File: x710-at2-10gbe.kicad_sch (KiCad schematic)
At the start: 18 parts, among them U4 EZX710AT2_S_LMR5

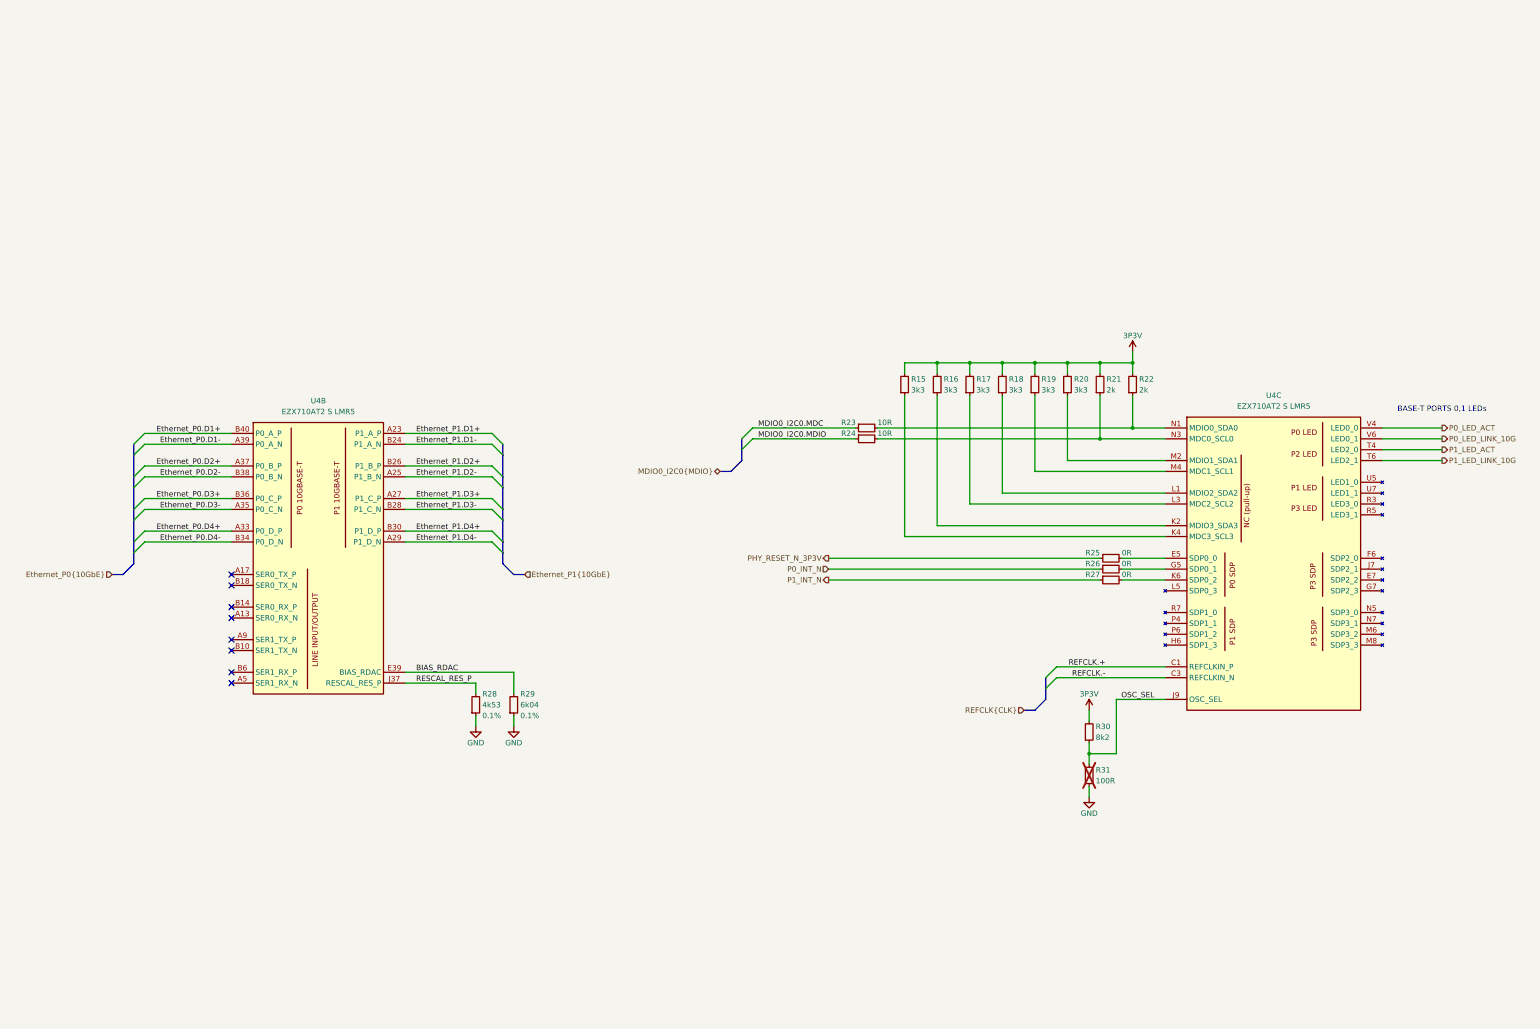
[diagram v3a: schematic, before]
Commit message: [#80813] Improve schematic readability, add debug connectors and missing resistors
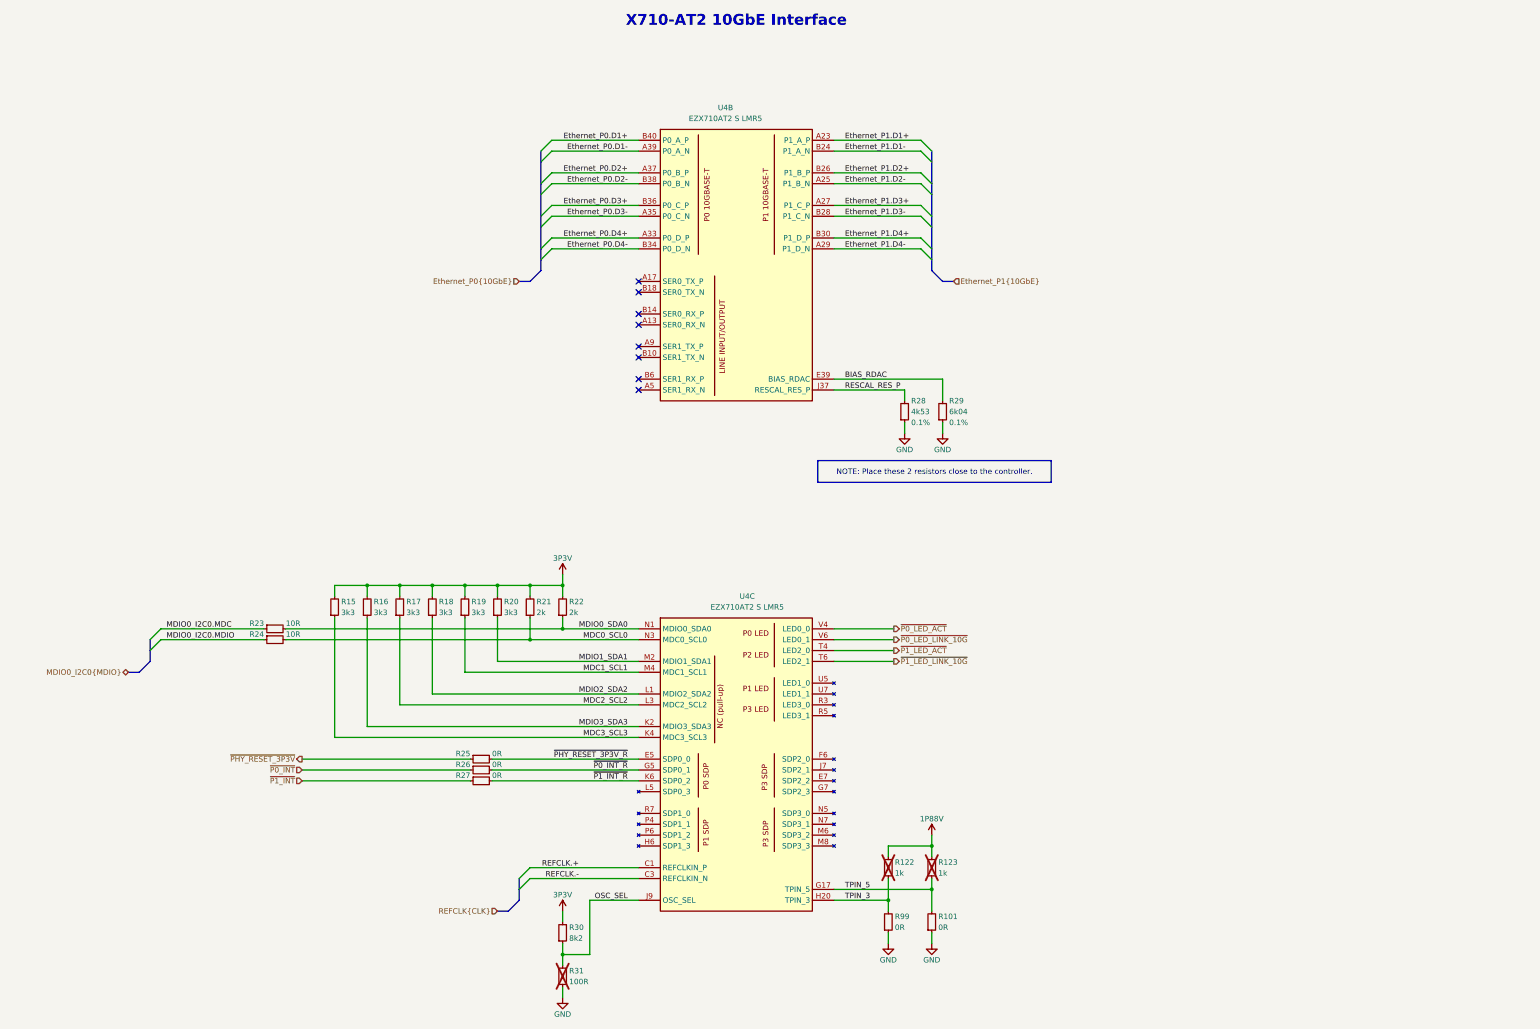
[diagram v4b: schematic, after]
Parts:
- added R101, R99: R_0R_0402, antmicro-footprints:R_0402_1005Metric, symbol antmicroResistors0402:R_0R_0402
- added R122, R123: R_1k_0402, antmicro-footprints:R_0402_1005Metric, symbol antmicroResistors0402:R_1k_0402
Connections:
- net GND: now also R101.1, R99.1
- net ~{P1_INT_R}: now reaches R27.2, U4.K6 (SDP0_2)
- net MDC1_SCL1: now reaches R19.1, U4.M4 (MDC1_SCL1)
- net ~{P0_INT_R}: now reaches R26.2, U4.G5 (SDP0_1)
- net MDC0_SCL0: now reaches R21.1, R24.2, U4.N3 (MDC0_SCL0)
- net MDIO0_SDA0: now reaches R22.1, R23.2, U4.N1 (MDIO0_SDA0)
- net MDIO2_SDA2: now reaches R18.1, U4.L1 (MDIO2_SDA2)
- net ~{PHY_RESET_3P3V_R}: now reaches R25.2, U4.E5 (SDP0_0)
- net MDIO3_SDA3: now reaches R16.1, U4.K2 (MDIO3_SDA3)
- net MDC3_SCL3: now reaches R15.1, U4.K4 (MDC3_SCL3)
- net MDC2_SCL2: now reaches R17.1, U4.L3 (MDC2_SCL2)
- net MDIO1_SDA1: now reaches R20.1, U4.M2 (MDIO1_SDA1)
- net P0_INT_N renamed ~{P0_INT}
- net P0_LED_ACT renamed ~{P0_LED_ACT}
- net P0_LED_LINK_10G renamed ~{P0_LED_LINK_10G}
- net P1_INT_N renamed ~{P1_INT}
- net P1_LED_ACT renamed ~{P1_LED_ACT}
- net P1_LED_LINK_10G renamed ~{P1_LED_LINK_10G}
- net PHY_RESET_N_3P3V renamed ~{PHY_RESET_3P3V}
- new net 1P88V: R122.2, R123.2
- new net TPIN_3: R122.1, R99.2, U4.H20 (TPIN_3)
- new net TPIN_5: R101.2, R123.1, U4.G17 (TPIN_5)
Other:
- note added: "X710-AT2 10GbE Interface"
- note removed: "BASE-T PORTS 0,1 LEDs"
- moved on the sheet: R15, R16, R17, R18, R19, R20, R21, R22, R23, R24, R25, R26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

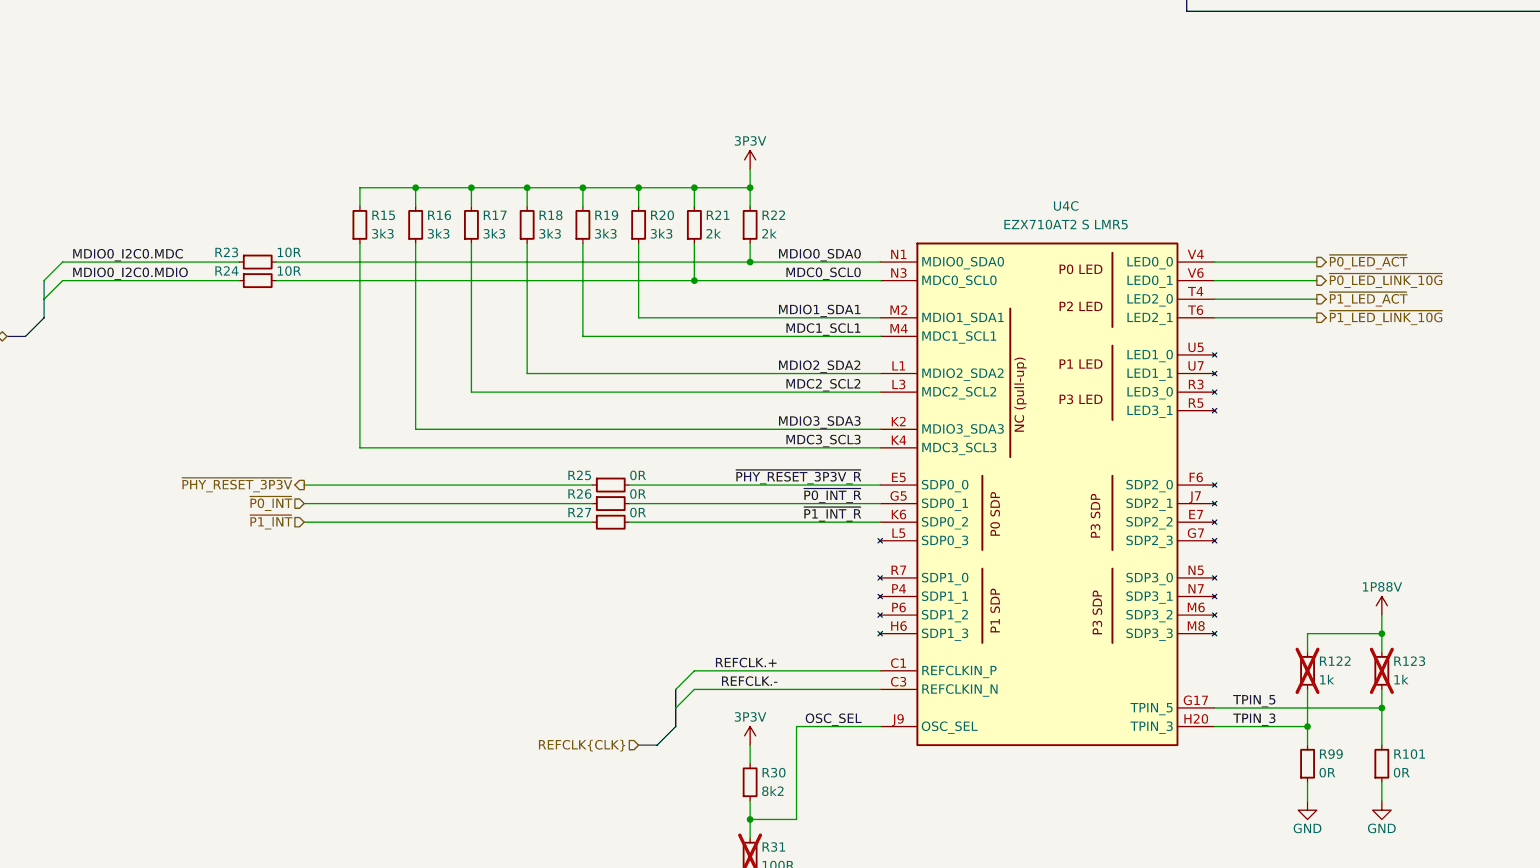
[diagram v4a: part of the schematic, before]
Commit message: [#80813] Change 3V3 and 1V88 power rails names
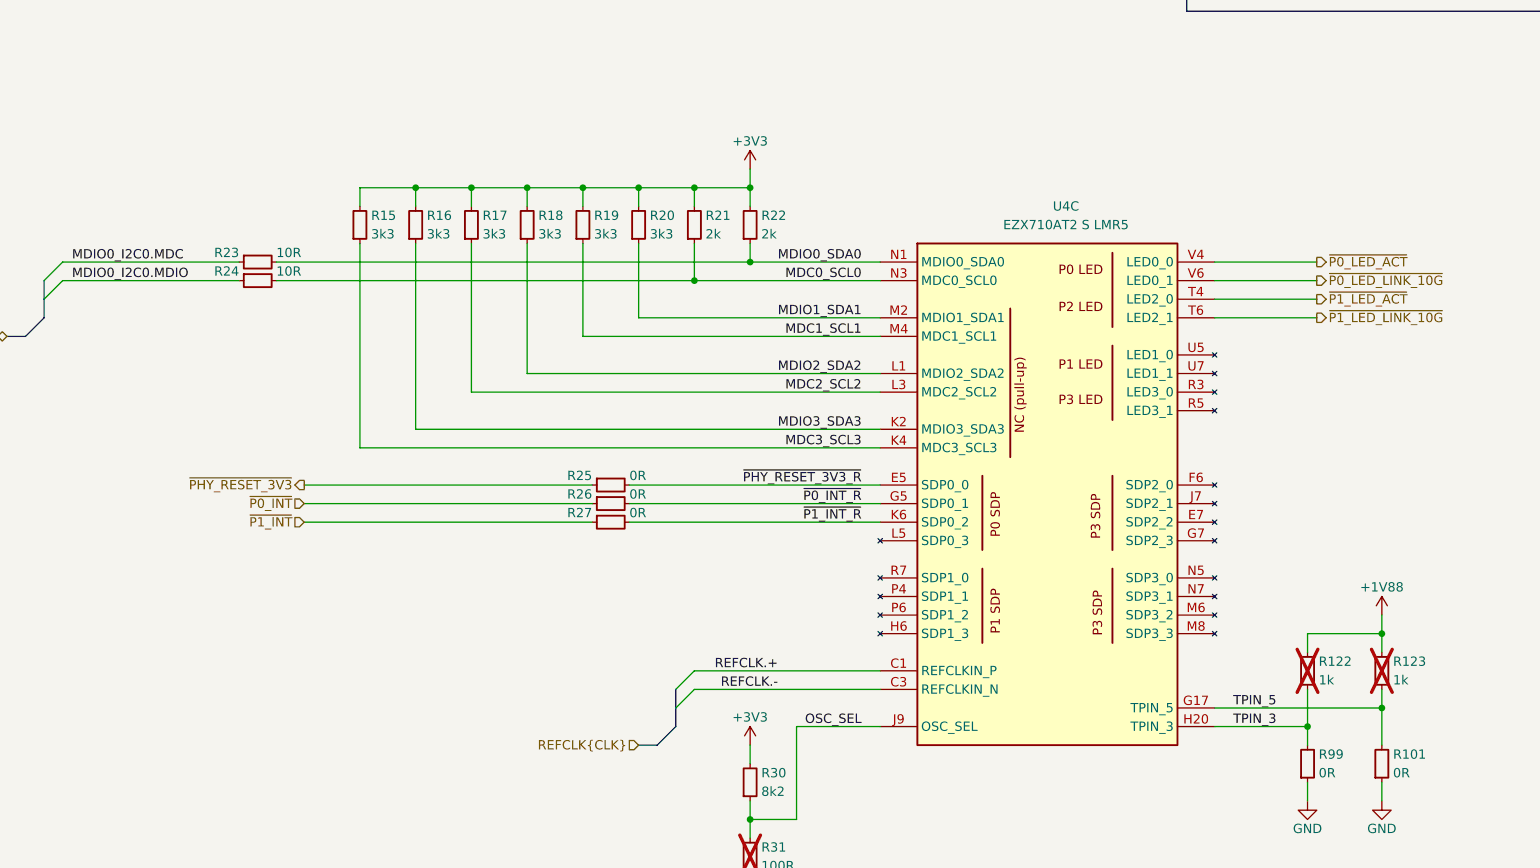
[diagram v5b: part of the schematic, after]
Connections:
- net 1P88V renamed +1V88
- net 3P3V renamed +3V3
- net ~{PHY_RESET_3P3V_R} renamed ~{PHY_RESET_3V3_R}
- net ~{PHY_RESET_3P3V} renamed ~{PHY_RESET_3V3}

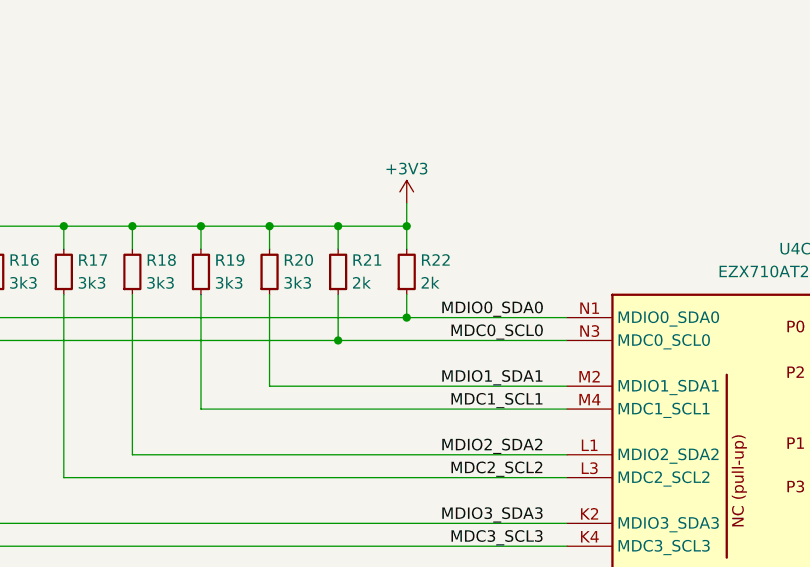
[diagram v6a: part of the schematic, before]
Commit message: [#80813] Adjust passives values, add remaining decoupling capacitors
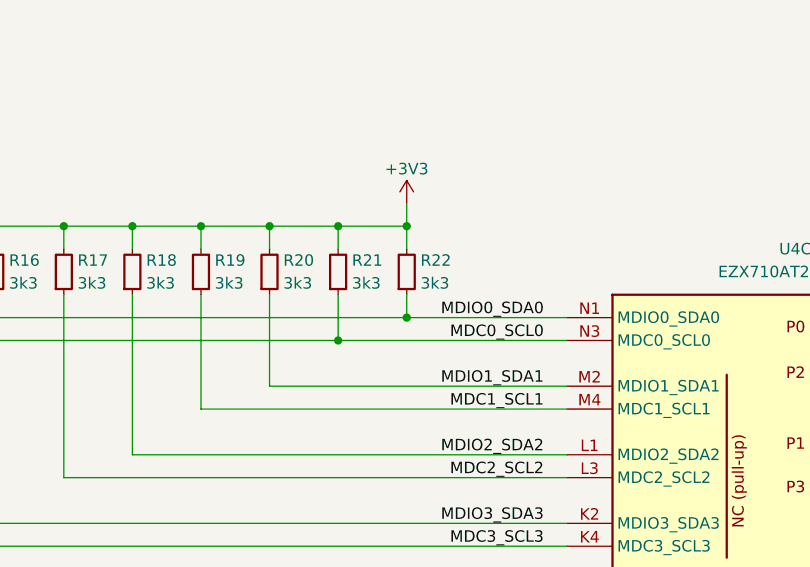
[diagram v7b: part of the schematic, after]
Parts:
- removed R21, R22: R_2k_0402, antmicro-footprints:R_0402_1005Metric, symbol antmicroResistors0402:R_2k_0402
- added R21, R22: R_3k3_0402, antmicro-footprints:R_0402_1005Metric, symbol antmicroResistors0402:R_3k3_0402
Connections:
- net +3V3: now also R21.2, R22.2
- net MDC0_SCL0: now also R21.1
- net MDIO0_SDA0: now also R22.1
